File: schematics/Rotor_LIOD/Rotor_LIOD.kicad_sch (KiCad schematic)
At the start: 177 parts, among them J1 2° drum photointerrupter, J1 8051 module connector, J10 Card slot solenoid, J11 First head, J12 ., J13 8051 interface, J1A Second head, J2 Drum entrance photointerrupter, J3 LIOD interface, J4 Card exit photointerrupter, J5 Main motor, J6 Drum 4° photointerrupter, J6A Third head, J7 Drum 3° photointerrupter, J8 Bottom LED, J9 Out of service LED, Q1 4 MHz, T1 BC817, T10 BC817, T11 BC817, T12 BC817, T13 BC817, T14 BC817, T2 BC817, T3 VN2406, T4 BC817, T5 BC807, T6 BC817, T7 BC817, T8 BC817, T9 BC817, U1 HD6305Y2, U1 S-80C51CCNW-12, U10 "Y306", U11 "312", U12 "312", U13 CD4052B, U14 CD4052B, U16 LM324, U17 CD4052B, U2 27C256, U2 LM385M-ADJ, U3 74HC244, U4 PLCC44, U5 LM339, U6 LP2951-5.0_SOIC, U7 "312", U8 "312", U9 40106

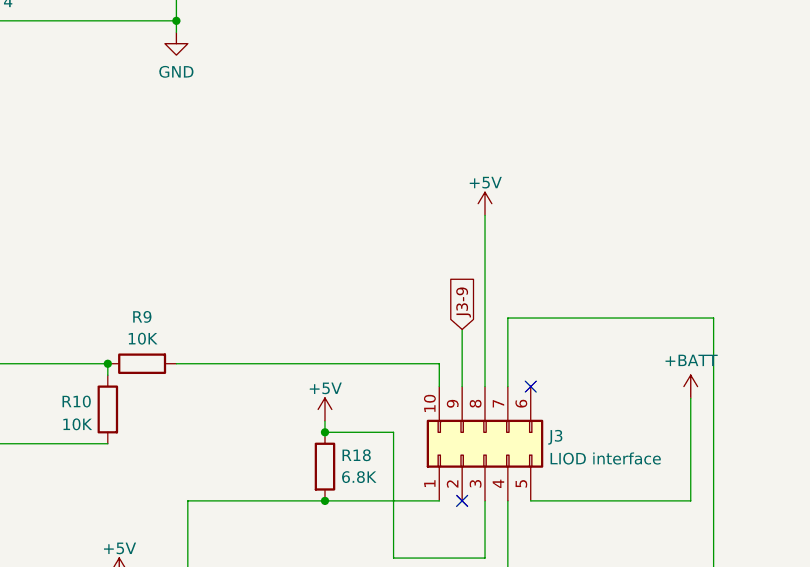
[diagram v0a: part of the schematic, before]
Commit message: Fixed a minor issue with the LIOD schematic
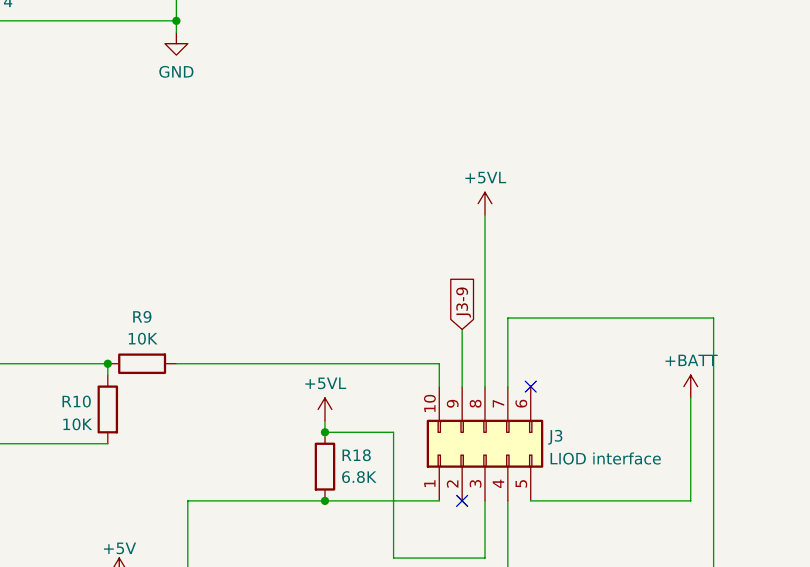
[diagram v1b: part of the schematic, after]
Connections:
- net +5V: no longer J3.3 (Pin_3), J3.8 (Pin_8), R18.1
- new net +5VL: J3.3 (Pin_3), J3.8 (Pin_8), R18.1
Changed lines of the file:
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@@
     )
   )
+  (symbol (lib_id "power:+5VL") (at -13.97 -138.43 0) (unit 1)
+    (in_bom yes) (on_board yes) (dnp no) (fields_autoplaced)
+    (property "Reference" "#PWR033" (at -13.97 -134.62 0)
+      (effects (font (size 1.27 1.27)) hide)
+    )
+    (property "Value" "+5VL" (at -13.97 -142.5631 0)
+      (effects (font (size 1.27 1.27)))
+    )
+    (property "Footprint" "" (at -13.97 -138.43 0)
+      (effects (font (size 1.27 1.27)) hide)
+    )
+    (property "Datasheet" "" (at -13.97 -138.43 0)
+      (effects (font (size 1.27 1.27)) hide)
+    )
+    (pin "1")
+    (instances
+      (project "Rotor_LIOD"
+        (path "/4a63612f-df1f-4e14-97e7-35aed46eab3f"
+          (reference "#PWR033") (unit 1)
+        )
+      )
+    )
+  )
   (symbol (lib_id "Device:R") (at 601.98 -267.97 270) (unit 1)
     (in_bom yes) (on_board yes) (dnp no) (fields_autoplaced)
@@
     )
   )
-  (symbol (lib_id "power:+5V") (at -13.97 -138.43 0) (unit 1)
-    (in_bom yes) (on_board yes) (dnp no) (fields_autoplaced)
-    (property "Reference" "#PWR033" (at -13.97 -134.62 0)
-      (effects (font (size 1.27 1.27)) hide)
-    )
-    (property "Value" "+5V" (at -13.97 -142.0058 0)
-      (effects (font (size 1.27 1.27)))
-    )
-    (property "Footprint" "" (at -13.97 -138.43 0)
-      (effects (font (size 1.27 1.27)) hide)
-    )
-    (property "Datasheet" "" (at -13.97 -138.43 0)
-      (effects (font (size 1.27 1.27)) hide)
-    )
-    (pin "1")
-    (instances
-      (project "Rotor_LIOD"
-        (path "/4a63612f-df1f-4e14-97e7-35aed46eab3f"
-          (reference "#PWR033") (unit 1)
-        )
-      )
-    )
-  )
   (symbol (lib_id "power:+5V") (at -36.83 -120.65 0) (unit 1)
     (in_bom yes) (on_board yes) (dnp no) (fields_autoplaced)
@@
     )
   )
+  (symbol (lib_id "power:+5VL") (at 3.81 -161.29 0) (unit 1)
+    (in_bom yes) (on_board yes) (dnp no) (fields_autoplaced)
+    (property "Reference" "#PWR043" (at 3.81 -157.48 0)
+      (effects (font (size 1.27 1.27)) hide)
+    )
+    (property "Value" "+5VL" (at 3.81 -165.4231 0)
+      (effects (font (size 1.27 1.27)))
+    )
+    (property "Footprint" "" (at 3.81 -161.29 0)
+      (effects (font (size 1.27 1.27)) hide)
+    )
+    (property "Datasheet" "" (at 3.81 -161.29 0)
+      (effects (font (size 1.27 1.27)) hide)
+    )
+    (pin "1")
+    (instances
+      (project "Rotor_LIOD"
+        (path "/4a63612f-df1f-4e14-97e7-35aed46eab3f"
+          (reference "#PWR043") (unit 1)
+        )
+      )
+    )
+  )
   (symbol (lib_id "power:GND") (at -13.97 -280.67 0) (unit 1)
     (in_bom yes) (on_board yes) (dnp no) (fields_autoplaced)
@@
         )
       )
-    )
-  )
-  (symbol (lib_id "power:+5V") (at 3.81 -161.29 0) (unit 1)
-    (in_bom yes) (on_board yes) (dnp no) (fields_autoplaced)
-    (property "Reference" "#PWR03" (at 3.81 -157.48 0)
-      (effects (font (size 1.27 1.27)) hide)
-    )
-    (property "Value" "+5V" (at 3.81 -164.8658 0)
-      (effects (font (size 1.27 1.27)))
-    )
-    (property "Footprint" "" (at 3.81 -161.29 0)
-      (effects (font (size 1.27 1.27)) hide)
-    )
-    (property "Datasheet" "" (at 3.81 -161.29 0)
-      (effects (font (size 1.27 1.27)) hide)
-    )
-    (pin "1")
-    (instances
-      (project "Rotor_LIOD"
-        (path "/4a63612f-df1f-4e14-97e7-35aed46eab3f"
-          (reference "#PWR03") (unit 1)
-        )
-      )
